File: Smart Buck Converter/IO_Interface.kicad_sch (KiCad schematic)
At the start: 18 parts, among them J1 691101710003, J2 PJ-063AH, J3 USB4105-GF-A, J4 PJ-063AH, J5 SHF-105-01-L-D-SM, J6 PJ-063AH, J7 SM04B-SRSS-TB(LF)(SN), SW1 TL3342F160QG

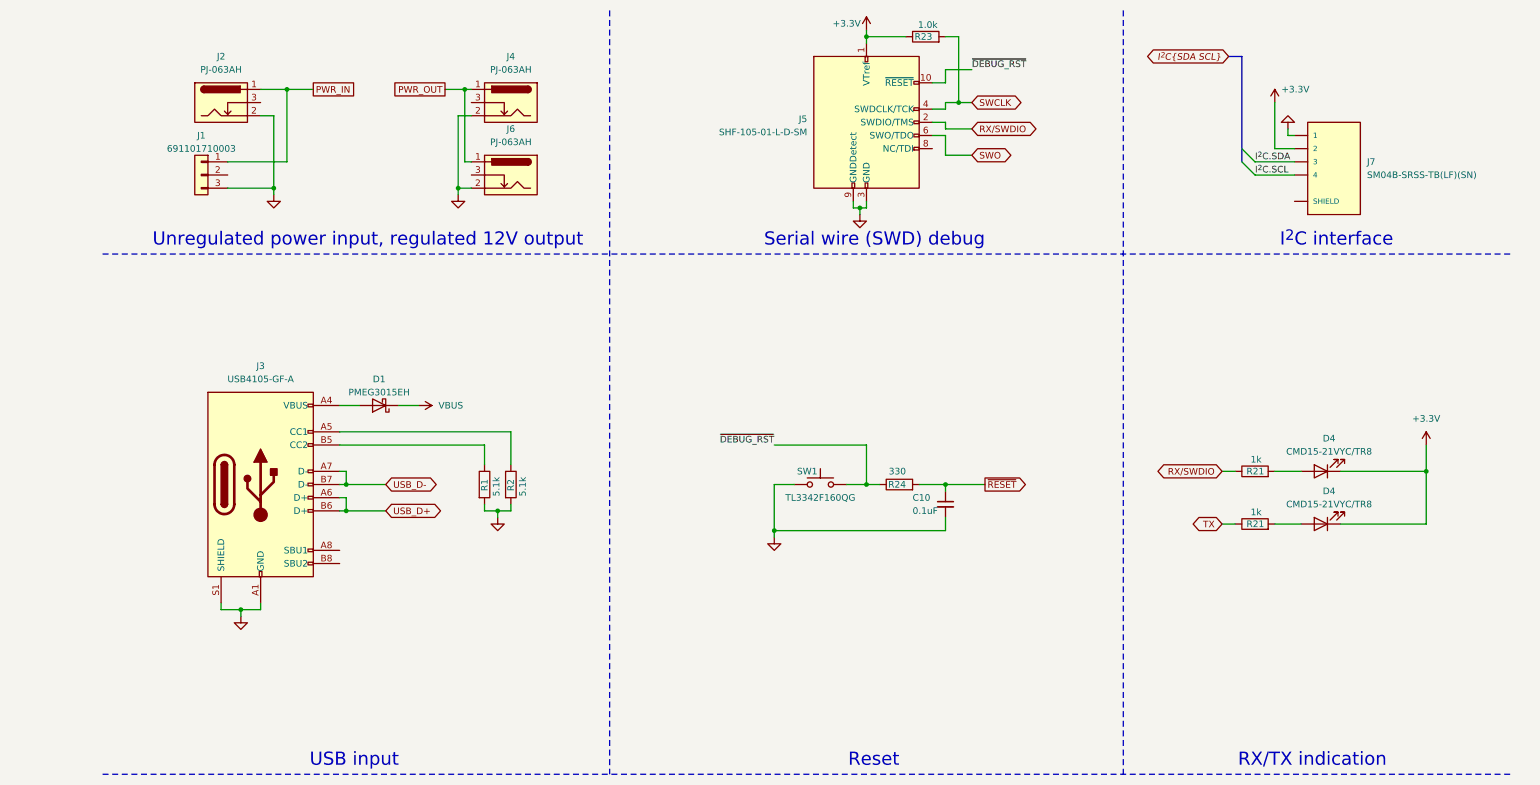
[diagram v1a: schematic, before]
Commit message: Revision 2 update
Regenerated gerber files to rev 2 design, made minor changes to PCB layout before exporting. Changed I2C interface connector from 4-pin right angle style to vertical style, added the new connector the the KiCad footprints library.
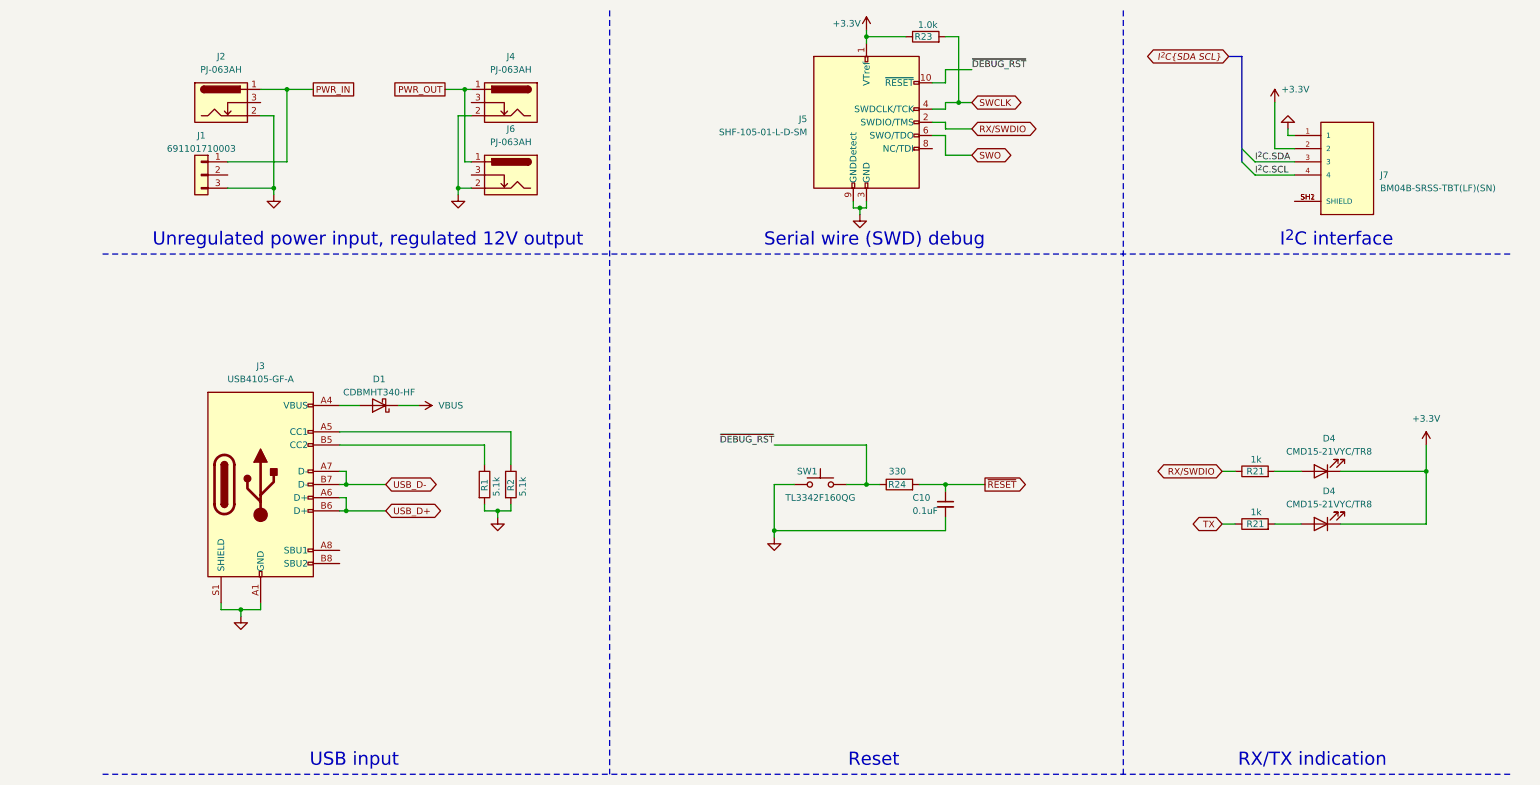
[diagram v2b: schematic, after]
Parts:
- D1: value PMEG3015EH -> CDBMHT340-HF
- J7: value SM04B-SRSS-TB(LF)(SN) -> BM04B-SRSS-TBT(LF)(SN); footprint JST_SM04B-SRSS-TB(LF)(SN) -> User Components:CONN_BM04B-SRSS-TBT(LF)(SN); symbol SM04B-SRSS-TB_LF__SN_:SM04B-SRSS-TB(LF)(SN) -> BM04B-SRSS-TBT_LF__SN_:BM04B-SRSS-TBT(LF)(SN)
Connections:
- new net: J7.SH1 (SHIELD), J7.SH2 (SHIELD)
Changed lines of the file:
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@@
     )
   )
-  (symbol (lib_id "SM04B-SRSS-TB_LF__SN_:SM04B-SRSS-TB(LF)(SN)") (at 250.19 41.91 0) (unit 1)
-    (in_bom yes) (on_board yes) (dnp no)
-    (property "Reference" "J7" (at 256.54 41.91 0)
-      (effects (font (size 1.27 1.27)) (justify left))
-    )
-    (property "Value" "SM04B-SRSS-TB(LF)(SN)" (at 256.54 44.45 0)
-      (effects (font (size 1.27 1.27)) (justify left))
-    )
-    (property "Footprint" "JST_SM04B-SRSS-TB(LF)(SN)" (at 250.19 41.91 0)
+  (symbol (lib_id "BM04B-SRSS-TBT_LF__SN_:BM04B-SRSS-TBT(LF)(SN)") (at 252.73 44.45 0) (unit 1)
+    (in_bom yes) (on_board yes) (dnp no)
+    (property "Reference" "J7" (at 259.08 44.45 0)
+      (effects (font (size 1.27 1.27)) (justify left))
+    )
+    (property "Value" "BM04B-SRSS-TBT(LF)(SN)" (at 259.08 46.99 0)
+      (effects (font (size 1.27 1.27)) (justify left))
+    )
+    (property "Footprint" "User Components:CONN_BM04B-SRSS-TBT(LF)(SN)" (at 252.73 44.45 0)
       (effects (font (size 1.27 1.27)) (justify bottom) hide)
     )
-    (property "Datasheet" "https://www.jst-mfg.com/product/pdf/eng/eSH.pdf" (at 250.19 41.91 0)
-      (effects (font (size 1.27 1.27)) hide)
-    )
-    (property "STANDARD" "Manufacturer recommendations" (at 250.19 41.91 0)
+    (property "Datasheet" "https://www.jst-mfg.com/product/pdf/eng/eSH.pdf" (at 252.73 44.45 0)
+      (effects (font (size 1.27 1.27)) hide)
+    )
+    (property "STANDARD" "Manufacturer recommendations" (at 252.73 44.45 0)
       (effects (font (size 1.27 1.27)) (justify bottom) hide)
     )
-    (property "MANUFACTURER" "JST" (at 250.19 41.91 0)
+    (property "MANUFACTURER" "JST" (at 252.73 44.45 0)
       (effects (font (size 1.27 1.27)) (justify bottom) hide)
     )
@@
     (pin "3")
     (pin "4")
-    (pin "S1")
-    (pin "S2")
+    (pin "SH1")
+    (pin "SH2")
     (instances
       (project "Smart Buck Converter"
@@
       (effects (font (size 1.27 1.27)))
     )
-    (property "Value" "PMEG3015EH" (at 66.04 86.36 0)
+    (property "Value" "CDBMHT340-HF" (at 66.04 86.36 0)
       (effects (font (size 1.27 1.27)))
     )
@@
       (effects (font (size 1.27 1.27)) hide)
     )
-    (property "Datasheet" "https://assets.nexperia.com/documents/data-sheet/PMEG3015EH_EJ.pdf" (at 66.04 88.9 0)
-      (effects (font (size 1.27 1.27)) hide)
-    )
+    (property "Datasheet" "https://www.mouser.com/datasheet/2/80/comchip_technology_comc-s-a0004994317-1-1734023.pdf" (at 66.04 88.9 0)
+      (effects (font (size 1.27 1.27)) hide)
+    )

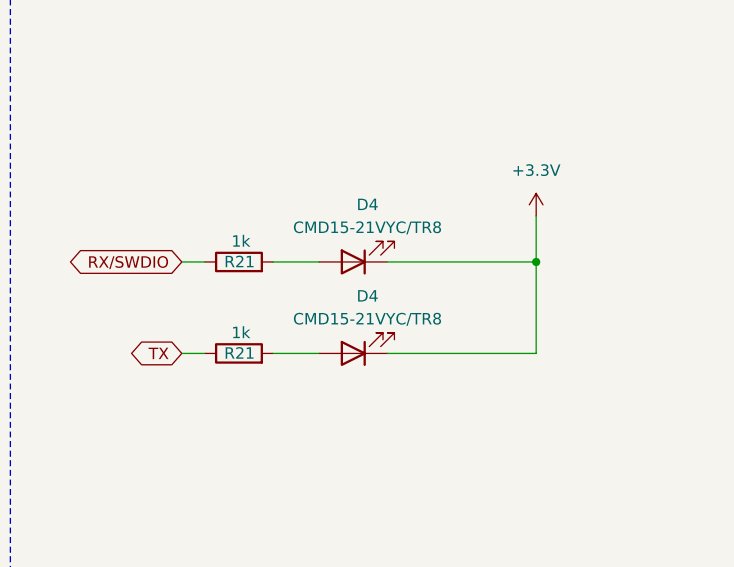
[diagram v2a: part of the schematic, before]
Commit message: Multiple updates
Added necessary code to support addition of either 128x64 or 128x32 OLED display from Adafruit. Fixed backwards polarity on RX/TX indicator LEDs. Updated enclosure to support addition of OLED display. Rendered shaded view of entire revision 2 assembly stack up. Generated BOM.
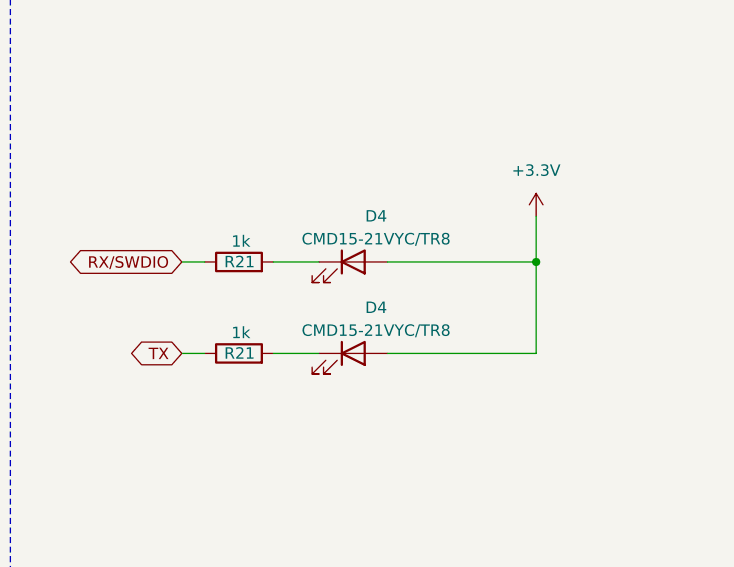
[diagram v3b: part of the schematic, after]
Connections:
- net +3V3: now also D4.2 (A), D4.2 (A); no longer D4.1 (K), D4.1 (K)
- net at R21.2: now also D4.1 (K); no longer D4.2 (A) (x2)
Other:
- moved on the sheet: D4
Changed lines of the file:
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@@
   (junction (at 48.26 27.94) (diameter 0) (color 0 0 0 0)
   )
+  (junction (at 160.02 104.14) (diameter 0) (color 0 0 0 0)
+  )
+  (junction (at 59.69 109.22) (diameter 0) (color 0 0 0 0)
+  )
+  (junction (at 142.24 113.03) (diameter 0) (color 0 0 0 0)
+  )
+  (junction (at 39.37 128.27) (diameter 0) (color 0 0 0 0)
+  )
+  (junction (at 160.02 17.78) (diameter 0) (color 0 0 0 0)
+  )
+  (junction (at 158.75 50.8) (diameter 0) (color 0 0 0 0)
+  )
+  (junction (at 59.69 104.14) (diameter 0) (color 0 0 0 0)
+  )
+  (junction (at 82.55 27.94) (diameter 0) (color 0 0 0 0)
+  )
   (junction (at 267.97 101.6) (diameter 0) (color 0 0 0 0)
-  )
-  (junction (at 160.02 104.14) (diameter 0) (color 0 0 0 0)
-  )
-  (junction (at 59.69 109.22) (diameter 0) (color 0 0 0 0)
-  )
-  (junction (at 142.24 113.03) (diameter 0) (color 0 0 0 0)
-  )
-  (junction (at 39.37 128.27) (diameter 0) (color 0 0 0 0)
-  )
-  (junction (at 160.02 17.78) (diameter 0) (color 0 0 0 0)
-  )
-  (junction (at 158.75 50.8) (diameter 0) (color 0 0 0 0)
-  )
-  (junction (at 59.69 104.14) (diameter 0) (color 0 0 0 0)
-  )
-  (junction (at 82.55 27.94) (diameter 0) (color 0 0 0 0)
   )
   (junction (at 88.9 109.22) (diameter 0) (color 0 0 0 0)
@@
     (stroke (width 0) (type default))
   )
-  (wire (pts (xy 267.97 96.52) (xy 267.97 101.6))
-    (stroke (width 0) (type default))
-  )
   (wire (pts (xy 58.42 109.22) (xy 59.69 109.22))
     (stroke (width 0) (type default))
@@
     (stroke (width 0) (type default))
   )
+  (wire (pts (xy 267.97 101.6) (xy 267.97 111.76))
+    (stroke (width 0) (type default))
+  )
   (wire (pts (xy 83.82 33.02) (xy 81.28 33.02))
     (stroke (width 0) (type default))
@@
     (stroke (width 0) (type default))
   )
+  (wire (pts (xy 238.76 101.6) (xy 243.84 101.6))
+    (stroke (width 0) (type default))
+  )
   (wire (pts (xy 157.48 49.53) (xy 157.48 50.8))
     (stroke (width 0) (type default))
@@
     (stroke (width 0) (type default))
   )
+  (wire (pts (xy 251.46 101.6) (xy 267.97 101.6))
+    (stroke (width 0) (type default))
+  )
+  (wire (pts (xy 251.46 111.76) (xy 267.97 111.76))
+    (stroke (width 0) (type default))
+  )
   (wire (pts (xy 88.9 109.22) (xy 91.44 109.22))
     (stroke (width 0) (type default))
@@
   )
   (wire (pts (xy 43.18 33.02) (xy 45.72 33.02))
-    (stroke (width 0) (type default))
-  )
-  (wire (pts (xy 238.76 111.76) (xy 243.84 111.76))
     (stroke (width 0) (type default))
   )
@@
     (stroke (width 0) (type default))
   )
-  (wire (pts (xy 251.46 101.6) (xy 267.97 101.6))
-    (stroke (width 0) (type default))
-  )
   (wire (pts (xy 59.69 109.22) (xy 67.31 109.22))
     (stroke (width 0) (type default))
@@
     (stroke (width 0) (type default))
   )
-  (wire (pts (xy 267.97 101.6) (xy 267.97 111.76))
+  (wire (pts (xy 267.97 96.52) (xy 267.97 101.6))
     (stroke (width 0) (type default))
   )
@@
     (stroke (width 0) (type default))
   )
-  (wire (pts (xy 267.97 111.76) (xy 251.46 111.76))
-    (stroke (width 0) (type default))
-  )
   (wire (pts (xy 160.02 17.78) (xy 167.64 17.78))
     (stroke (width 0) (type default))
@@
     (stroke (width 0) (type default))
   )
+  (wire (pts (xy 238.76 111.76) (xy 243.84 111.76))
+    (stroke (width 0) (type default))
+  )
   (wire (pts (xy 81.28 46.99) (xy 81.28 48.26))
     (stroke (width 0) (type default))
   )
   (wire (pts (xy 234.95 44.45) (xy 242.57 44.45))
-    (stroke (width 0) (type default))
-  )
-  (wire (pts (xy 238.76 101.6) (xy 243.84 101.6))
     (stroke (width 0) (type default))
   )
@@
     )
   )
-  (symbol (lib_id "Device:LED") (at 247.65 111.76 180) (unit 1)
-    (in_bom yes) (on_board yes) (dnp no) (fields_autoplaced)
-    (property "Reference" "D4" (at 249.2375 105.41 0)
-      (effects (font (size 1.27 1.27)))
-    )
-    (property "Value" "CMD15-21VYC/TR8" (at 249.2375 107.95 0)
+  (symbol (lib_id "Device:LED") (at 247.65 111.76 0) (unit 1)
+    (in_bom yes) (on_board yes) (dnp no)
+    (property "Reference" "D4" (at 250.19 106.68 0)
+      (effects (font (size 1.27 1.27)))
+    )
+    (property "Value" "CMD15-21VYC/TR8" (at 250.19 109.22 0)
       (effects (font (size 1.27 1.27)))
     )
@@
     )
   )
-  (symbol (lib_id "Device:LED") (at 247.65 101.6 180) (unit 1)
-    (in_bom yes) (on_board yes) (dnp no) (fields_autoplaced)
-    (property "Reference" "D4" (at 249.2375 95.25 0)
-      (effects (font (size 1.27 1.27)))
-    )
-    (property "Value" "CMD15-21VYC/TR8" (at 249.2375 97.79 0)
-      (effects (font (size 1.27 1.27)))
-    )
+  (symbol (lib_id "Device:LED") (at 247.65 101.6 0) (unit 1)
+    (in_bom yes) (on_board yes) (dnp no)
+    (property "Reference" "D4" (at 250.19 96.52 0)
+      (effects (font (size 1.27 1.27)))
+    )
+    (property "Value" "CMD15-21VYC/TR8" (at 250.19 99.06 0)
+      (effects (font (size 1.27 1.27)))
+    )
